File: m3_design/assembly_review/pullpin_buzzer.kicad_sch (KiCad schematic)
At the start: 10 parts, among them J123 PULL-PIN PH 1x2, Q123 AO3400A

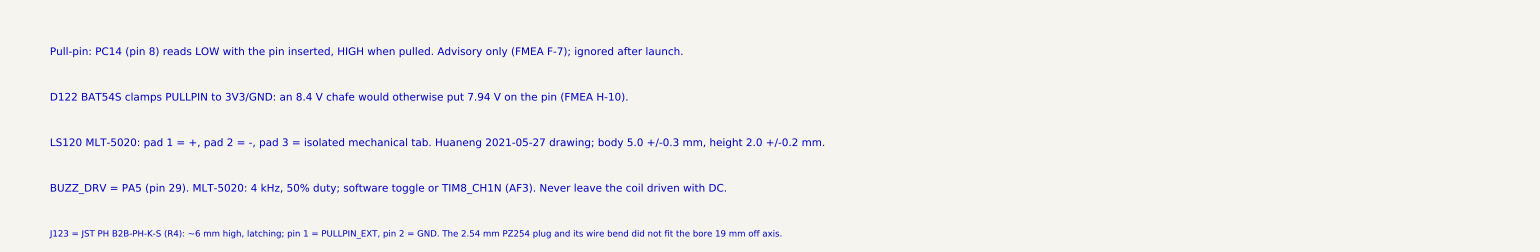
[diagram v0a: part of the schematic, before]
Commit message: M3-ASSY-R8: re-placed layout with planned-bus routing, owner-accepted deviations
R8 keeps R7's circuit, RF strip and CH1 pyro block (copied rigidly and
hash-asserted) and re-places everything else: U1 rotated so its free
pins face the RF strip, each block beside the U1 face it talks to, input
protection back at J1, and a fresh deterministic build (r8_build.sh)
with planned-bus routing, no autorouter and no patch stages.

Against R7: signal track 3.36 m -> 1.50 m, signal vias 217 -> 55,
simplicity index 100 -> 15.3, gate exceptions 74 -> 3, hard routing-rule
instances 10 -> 1, 7.7 A neck rise 38/30/44 -> 17.6/14.8/22.3 C,
unreferenced critical samples 27.9 % -> 11.1 %, non-pyro nets within
3 mm of armed copper 23 -> 7.

- Gate: check_r8 (pin contract from pin_table.tsv, F10 separation,
  battery/pyro clearance, loader-pin rule, rigid hashes), route_check
  profile r8, scorecard, dc_solve --necks, reference_audit, paste_check
- Review: passes 2, 3 and 4 found 0 Critical / 0 Major in all eight
  dimensions; pass 5 re-checked the final board (routing, planes,
  integrity) with 0 Critical / 0 Major
- Owner accepted the R8 deviation list on 2026-10-20, including the C10
  vibration item and the listed agent decisions

Board SHA-256 cc044ea0922ff826df19af9d9726d92c096ab2b127025b55d123d8772e5fb4a7.
tools/check.sh: DRC 0, unconnected 0, parity 0, ERC 0; audit, silk,
R8 contract, routing hygiene (0 failing, 3 allowlisted), actuator
contract and fit OK. Before ordering: consign U4, JLC tab acceptance,
cost/stock run within 24 h.

Co-Authored-By: Claude Opus 5.5 <noreply@anthropic.com>
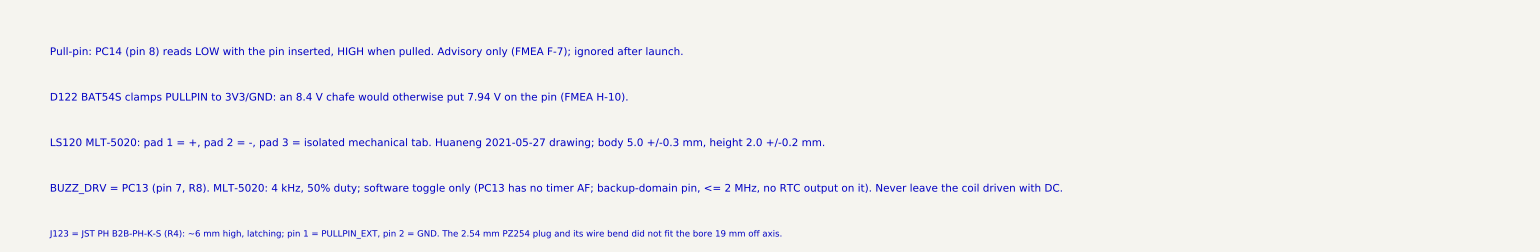
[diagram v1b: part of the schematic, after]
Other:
- note added: "BUZZ_DRV = PC13 (pin 7, R8). MLT-5020: 4 kHz, 50% duty; software toggle only (PC13 has no timer AF; backup-domain pin, <= 2 MHz, no RTC output on it). Never leave the coil driven with DC."
- note removed: "BUZZ_DRV = PA5 (pin 29). MLT-5020: 4 kHz, 50% duty; software toggle or TIM8_CH1N (AF3). Never leave the coil driven with DC."
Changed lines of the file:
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@@
 		(title "14 | Launch pull-pin and buzzer")
 		(date "2026-09-25")
-		(rev "M3-ASSY-R7")
+		(rev "M3-ASSY-R8")
 		(company "Single-board M3 candidate; actuator merge, not bench-verified"))
 	(symbol
@@
 			(justify left))
 )
-	(text "BUZZ_DRV = PA5 (pin 29). MLT-5020: 4 kHz, 50% duty; software toggle or TIM8_CH1N (AF3). Never leave the coil driven with DC."
+	(text "BUZZ_DRV = PC13 (pin 7, R8). MLT-5020: 4 kHz, 50% duty; software toggle only (PC13 has no timer AF; backup-domain pin, <= 2 MHz, no RTC output on it). Never leave the coil driven with DC."
 		(at 20.32 267.86 0)
 		(effects

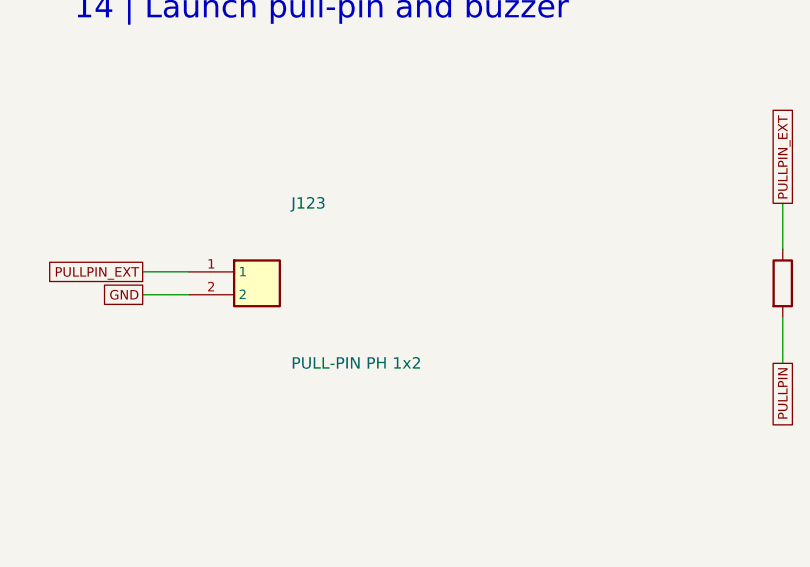
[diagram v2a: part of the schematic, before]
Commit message: R10: m3_design/r10_build.sh and per-family stage gate; m3_design/assembly_review rebuilt as M3-ASSY-R10 (board 883d2db5..., 46 x 90 mm); tools/check.sh passes at zero; binding note bound to the board
Co-Authored-By: Claude Opus 5.5 <noreply@anthropic.com>
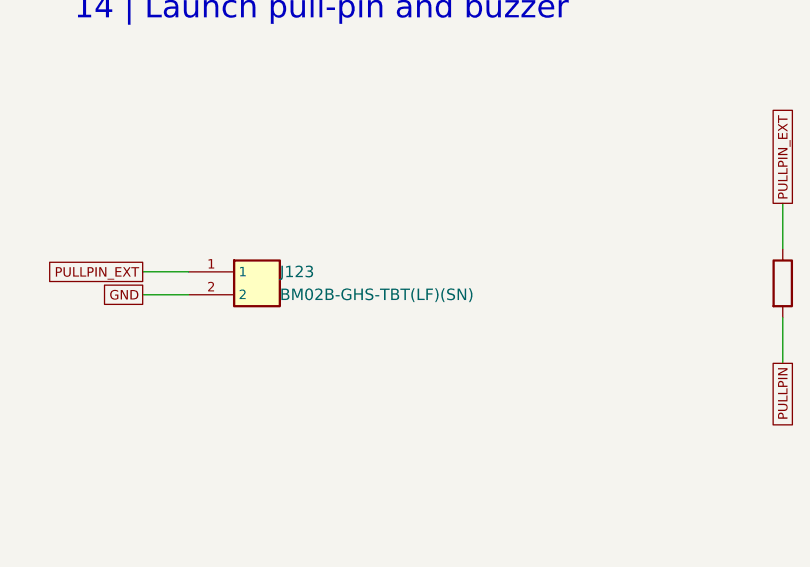
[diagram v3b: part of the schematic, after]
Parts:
- J123: value PULL-PIN PH 1x2 -> BM02B-GHS-TBT(LF)(SN); footprint rocket:M3_JST_PH_B2B_2P -> rocket:M3_GH_BM02B_GHS_TBT; LCSC C131337 -> C161690; LCSC Part C131337 -> (none); Manufacturer Part B2B-PH-K-S(LF)(SN) -> BM02B-GHS-TBT(LF)(SN)
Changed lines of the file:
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@@
 		(title "14 | Launch pull-pin and buzzer")
 		(date "2026-09-25")
-		(rev "M3-ASSY-R9")
+		(rev "M3-ASSY-R10")
 		(company "Single-board M3 candidate; actuator merge, not bench-verified"))
-	(symbol
-		(lib_id "M3:Conn_1x2")
-		(at 40.64 50.8 0)
-		(unit 1)
-		(in_bom yes)
-		(on_board yes)
-		(dnp no)
-		(property "Reference" "J123"
-			(at 44.45 41.91 0)
-			(effects
-				(font
-					(size 1.27 1.27))
-				(justify left)))
-		(property "Value" "PULL-PIN PH 1x2"
-			(at 44.45 59.69 0)
-			(effects
-				(font
-					(size 1.27 1.27))
-				(justify left)))
-		(property "Footprint" "rocket:M3_JST_PH_B2B_2P"
-			(at 40.64 50.8 0)
-			(hide yes)
-			(effects
-				(font
-					(size 1.27 1.27))))
-		(property "Datasheet" ""
-			(at 40.64 50.8 0)
-			(hide yes)
-			(effects
-				(font
-					(size 1.27 1.27))))
-		(property "LCSC" "C131337"
-			(at 40.64 50.8 0)
-			(hide yes)
-			(effects
-				(font
-					(size 1.27 1.27))))
-		(property "LCSC Part" "C131337"
-			(at 40.64 50.8 0)
-			(hide yes)
-			(effects
-				(font
-					(size 1.27 1.27))))
-		(property "Manufacturer" "JST"
-			(at 40.64 50.8 0)
-			(hide yes)
-			(effects
-				(font
-					(size 1.27 1.27))))
-		(property "Manufacturer Part" "B2B-PH-K-S(LF)(SN)"
-			(at 40.64 50.8 0)
-			(hide yes)
-			(effects
-				(font
-					(size 1.27 1.27))))
-		(instances
-			(project "m3"
-				(path "/6007a7db-6a58-5660-8beb-956dea045ff8/5ee931eb-d962-5c64-b0fd-46233c13323f"
-					(reference "J123")
-					(unit 1)))))
-	(wire
-		(pts
-			(xy 33.02 49.53)
-			(xy 27.94 49.53))
-		(stroke
-			(width 0)
-			(type default))
-)
-	(global_label "PULLPIN_EXT"
-		(shape passive)
-		(at 27.94 49.53 180)
-		(effects
-			(font
-				(size 1.05 1.05))
-			(justify right))
-)
-	(wire
-		(pts
-			(xy 33.02 52.07)
-			(xy 27.94 52.07))
-		(stroke
-			(width 0)
-			(type default))
-)
-	(global_label "GND"
-		(shape passive)
-		(at 27.94 52.07 180)
-		(effects
-			(font
-				(size 1.05 1.05))
-			(justify right))
-)
 	(symbol
 		(lib_id "M3:R")
@@
 			(justify left))
 )
+	(symbol
+		(lib_id "M3:Conn_1x2")
+		(at 40.64 50.8 0)
+		(unit 1)
+		(in_bom yes)
+		(on_board yes)
+		(dnp no)
+		(property "Reference" "J123"
+			(at 43.18 49.53 0)
+			(effects
+				(font
+					(size 1.27 1.27))
+				(justify left)))
+		(property "Value" "BM02B-GHS-TBT(LF)(SN)"
+			(at 43.18 52.07 0)
+			(effects
+				(font
+					(size 1.27 1.27))
+				(justify left)))
+		(property "Footprint" "rocket:M3_GH_BM02B_GHS_TBT"
+			(at 40.64 50.8 0)
+			(hide yes)
+			(effects
+				(font
+					(size 1.27 1.27))
+				(justify left)))
+		(property "Datasheet" "https://www.jst-mfg.com/product/pdf/eng/eGH.pdf"
+			(at 40.64 50.8 0)
+			(hide yes)
+			(effects
+				(font
+					(size 1.27 1.27))
+				(justify left)))
+		(property "LCSC" "C161690"
+			(at 40.64 50.8 0)
+			(hide yes)
+			(effects
+				(font
+					(size 1.27 1.27))
+				(justify left)))
+		(property "Manufacturer" "JST"
+			(at 40.64 50.8 0)
+			(hide yes)
+			(effects
+				(font
+					(size 1.27 1.27))
+				(justify left)))
+		(property "Manufacturer Part" "BM02B-GHS-TBT(LF)(SN)"
+			(at 40.64 50.8 0)
+			(hide yes)
+			(effects
+				(font
+					(size 1.27 1.27))
+				(justify left)))
+		(instances
+			(project "m3"
+				(path "/6007a7db-6a58-5660-8beb-956dea045ff8/5ee931eb-d962-5c64-b0fd-46233c13323f"
+					(reference "J123")
+					(unit 1)))))
+	(wire
+		(pts
+			(xy 33.02 49.53)
+			(xy 27.94 49.53))
+		(stroke
+			(width 0)
+			(type default))
+)
+	(global_label "PULLPIN_EXT"
+		(shape passive)
+		(at 27.94 49.53 0)
+		(effects
+			(font
+				(size 1.05 1.05))
+			(justify right))
+)
+	(wire
+		(pts
+			(xy 33.02 52.07)
+			(xy 27.94 52.07))
+		(stroke
+			(width 0)
+			(type default))
+)
+	(global_label "GND"
+		(shape passive)
+		(at 27.94 52.07 0)
+		(effects
+			(font
+				(size 1.05 1.05))
+			(justify right))
+)
 	(sheet_instances
